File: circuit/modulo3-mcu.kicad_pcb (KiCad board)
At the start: 2 copper layers, 87 x 52 mm, 46 parts, among them Q1 BS250, Q2 BS170, U1 74LVC2G32DC, U10 PWR_CONN, U11 FOOTSWITCH, U2 AVR64DA64, U3 SN74LVC1G17, U4 UPDI, U5 TOUCHSCREEN_240x320, U6 FV1_CONN, U7 DBG_UART, U8 AMPCTRL, Y1 32768Hz

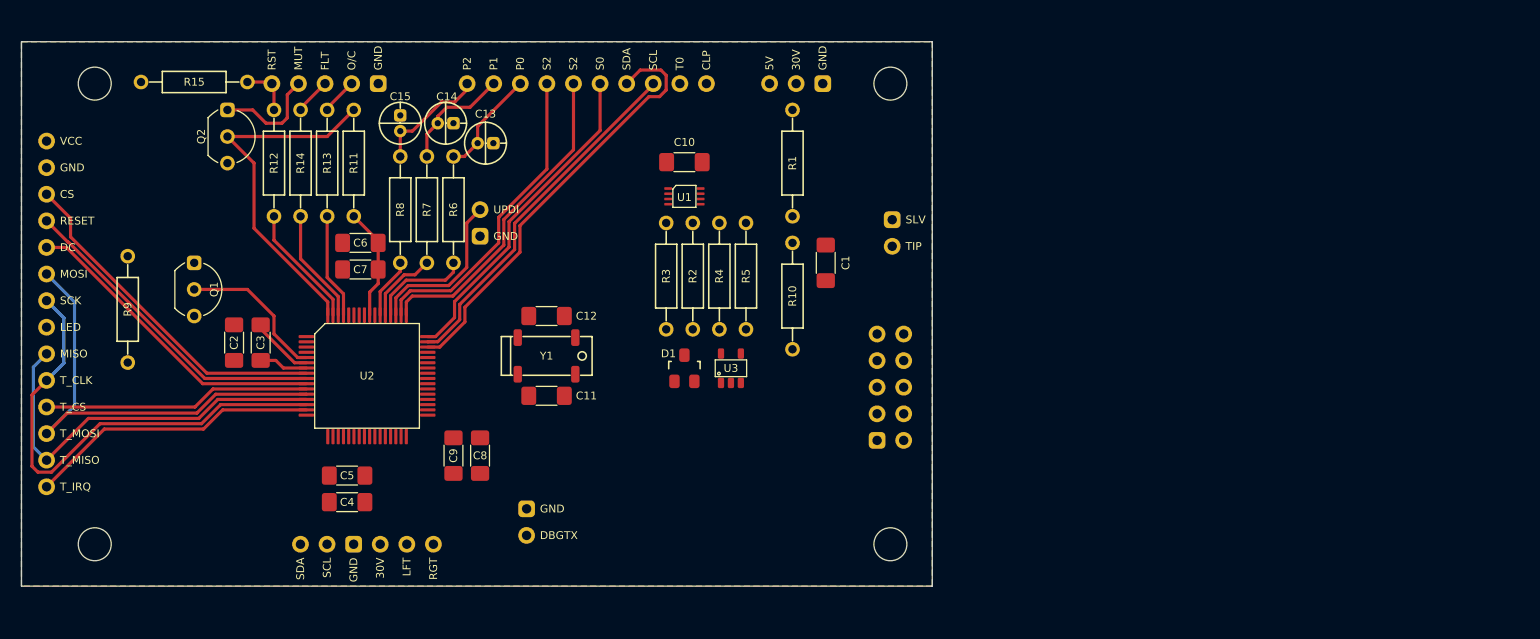
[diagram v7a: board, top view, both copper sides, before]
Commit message: mcu pcb first draft done!
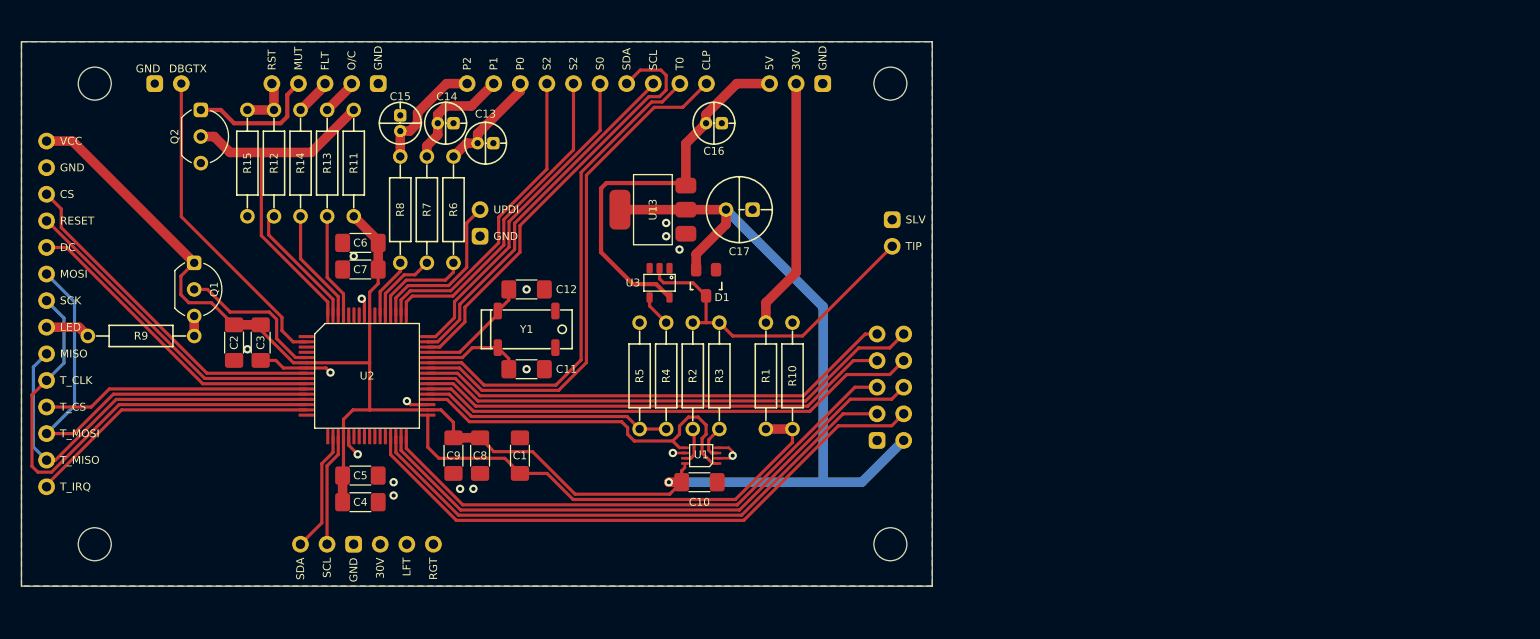
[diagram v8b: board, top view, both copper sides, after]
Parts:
- added C16: 10µF, myAmp:CPOL_D4_P1.5, F.Cu at (113.1, 57.8)
- added C17: 100µF, myAmp:CPOL_D6.3_P2.5, F.Cu at (115.6, 66.0)
- added U13: LM1117 3V3, myAmp:SOT-223, F.Cu at (107.3, 66.0)
- moved U7 54.1 mm to (61.0, 54.0), turned to 90 degrees
- moved C1 34.5 mm to (94.6, 89.5), turned to 90 degrees
- moved C10 30.6 mm to (111.8, 92.1), turned to 0 degrees
- moved U1 24.8 mm to (111.9, 89.5), turned to 180 degrees
- moved R1 20.5 mm to (118.1, 81.9)
- moved R5 13.9 mm to (106.0, 81.9), turned to 90 degrees
- moved R3 10.8 mm to (113.7, 81.9), turned to 90 degrees
- moved R4 10.8 mm to (108.6, 81.9), turned to -90 degrees
- moved U3 10.6 mm to (108.0, 73.0), turned to -90 degrees
- moved R2 9.53 mm to (111.1, 81.9), turned to 90 degrees
- moved R15 9.26 mm to (68.6, 61.6), turned to 90 degrees
- moved D1 8.42 mm to (112.4, 73.0), turned to 180 degrees
- moved R10 7.62 mm to (120.7, 81.9), turned to 90 degrees
- moved C12 3.18 mm to (95.2, 73.7)
- moved Y1 3.18 mm to (95.2, 77.5)
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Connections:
- U12 pad 2: /ADC0 -> /RE_A
- U12 pad 3: /ADC1 -> /RE_B
- U12 pad 4: /ADC2 -> /ADC1
- U12 pad 6: /RE_A -> /ADC2
- U12 pad 7: /RE_B -> /ADC0
- U12 pad 9: unconnected-(U12-N/C-Pad9) -> /RE_LED
- U2 pad 2: unconnected-(U2-PA4-Pad2) -> /DBG_TX
- U2 pad 29: unconnected-(U2-PD3-Pad29) -> /RE_LED
- U2 pad 30: unconnected-(U2-PD4-Pad30) -> /RE_A
- U2 pad 31: unconnected-(U2-PD5-Pad31) -> /RE_SW
- U2 pad 32: unconnected-(U2-PD6-Pad32) -> /RE_B
- U2 pad 33: unconnected-(U2-PD7-Pad33) -> /IN_V
- U2 pad 36: unconnected-(U2-PE0-Pad36) -> /FSTX
- U2 pad 37: unconnected-(U2-PE1-Pad37) -> /FSRX
- U2 pad 38: unconnected-(U2-PE2-Pad38) -> /ADC0
- U2 pad 39: unconnected-(U2-PE3-Pad39) -> /ADC1
- U2 pad 40: unconnected-(U2-PE4-Pad40) -> /ADC2
- U2 pad 41: unconnected-(U2-PE5-Pad41) -> /ADC3
- U2 pad 42: unconnected-(U2-PE6-Pad42) -> /FV_CLIP
- U2 pad 43: unconnected-(U2-PE7-Pad43) -> /T0
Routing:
- net +3.3V: track 16.8 -> 182.7 mm, vias 0 -> 1
- net /RE_LED: track 0.00 -> 57.6 mm
- net /RE_SW: track 0.00 -> 56.5 mm
- net /RE_A: track 0.00 -> 54.0 mm
- net /RE_B: track 0.00 -> 53.0 mm
- net /FV_CLIP: track 0.00 -> 50.1 mm
- net /ADC2: track 0.00 -> 49.0 mm
- net /ADC0: track 0.00 -> 48.4 mm
- net /T0: track 0.00 -> 47.4 mm
- net /ADC3: track 0.00 -> 46.3 mm
- net /IN_V: track 0.00 -> 46.0 mm
- net /ADC1: track 0.00 -> 45.6 mm
- net +5V: track 0.00 -> 37.7 mm
- net /FSTX: track 0.00 -> 36.5 mm
- net Net-(U11-TIP): track 0.00 -> 31.8 mm
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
